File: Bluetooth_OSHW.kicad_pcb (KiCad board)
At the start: 4 copper layers, 45.8 x 19.6 mm, 79 parts, among them J1 Conn_01x15, J2 Conn_01x15, J3 BAT_SOCKET, J4 Conn_ARM_SWD_TagConnect_TC203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, J5 USB_C_Plug_USB2.0, Q1 DMG1012T, U1 STM32WB55RGVx, U3 AT25SL321-U, U4 BQ25185, U5 TPS62746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

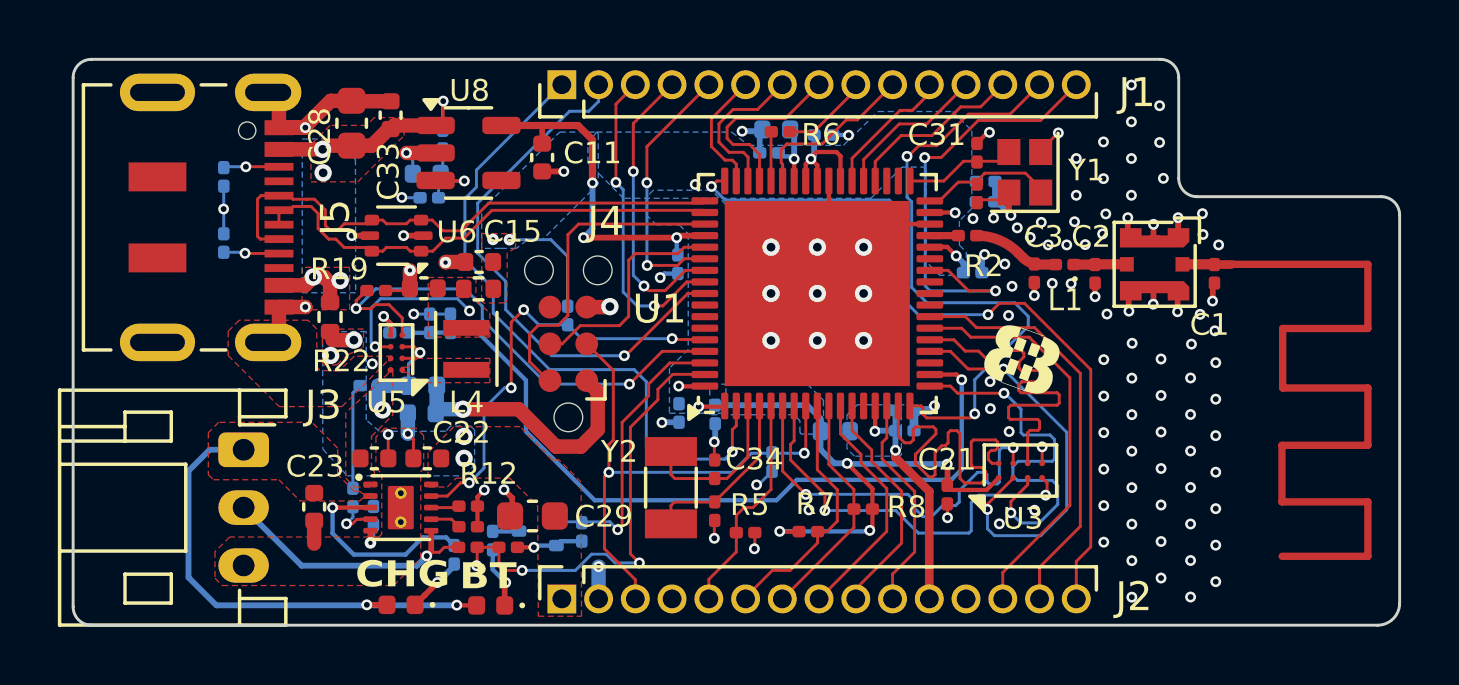
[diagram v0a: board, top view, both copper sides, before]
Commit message: Adding outputs, updated some component values.
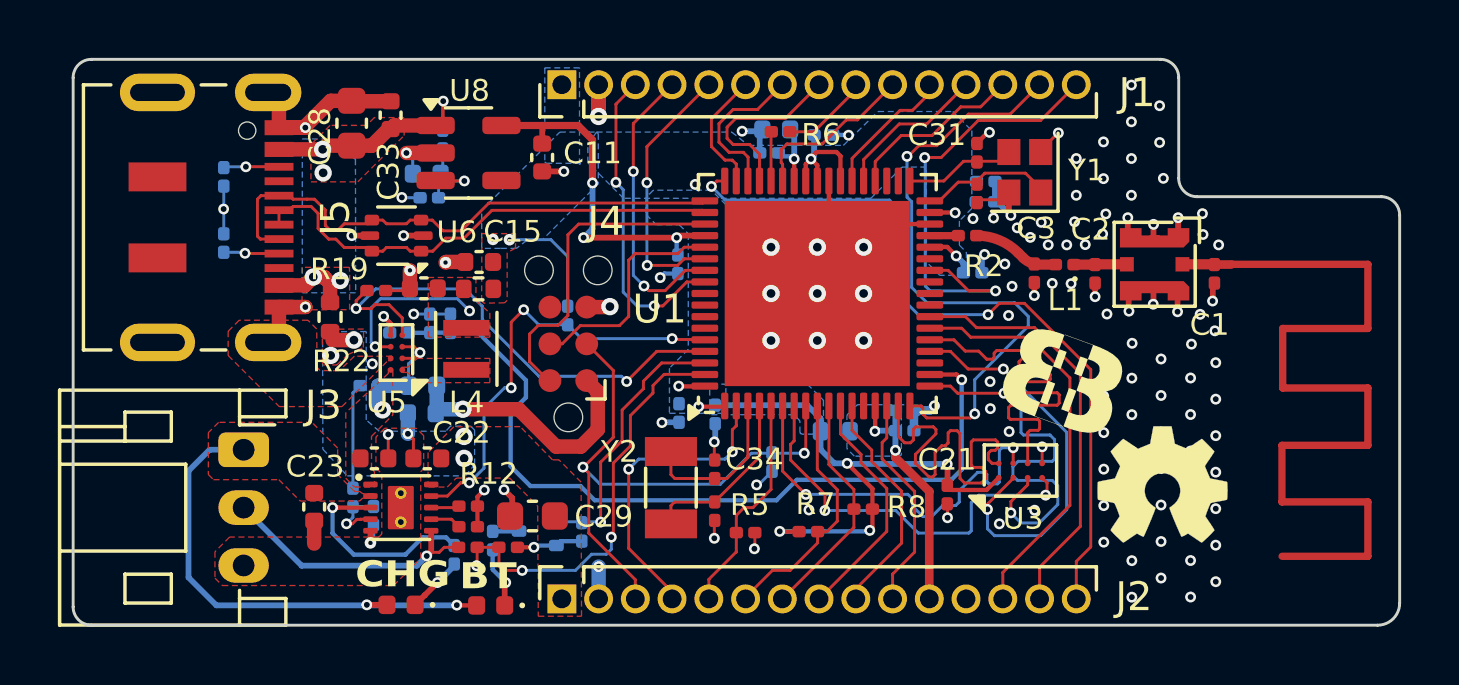
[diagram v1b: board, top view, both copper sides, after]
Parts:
- added REF**: OSHW-Logo_5.7x6mm_SilkScreen, Symbol:OSHW-Logo_5.7x6mm_SilkScreen, F.Cu at (229.0, 143.7)
- C11: value C -> 4.7UF
- D3: value D -> BAT54LP
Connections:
- J1 pad 1: STM_WKUP2_PC13 -> PP1800_ALW
- J1 pad 2: STM_WKUP3_PC12 -> GND
- J2 pad 4: unconnected-(J2-Pin_4-Pad4) -> STM_WKUP2_PC13
- U1 pad 60: STM_WKUP3_PC12 -> unconnected-(U1-PC12-Pad60)
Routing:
- net STM_WKUP3_PC12: track 18.7 -> 0.00 mm, vias 1 -> 0
- net STM_WKUP2_PC13: track 23.1 -> 10.6 mm, vias 1 -> 2
- net GND: track 62.7 -> 64.9 mm, vias 128 -> 129
- net RESETB: track 18.4 -> 20.4 mm
- net VIN_SNS_ADC1_IN9: track 27.3 -> 28.7 mm
- net BAT_CHRG_FACTORY: track 15.7 -> 14.5 mm
- net /BLE_MCU/BT_CONN_LED: track 10.0 -> 9.48 mm
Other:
- board text removed: "${REFERENCE}"

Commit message: updating design files
updating schematics, gerbers, design files, etc.
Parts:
- R16: value 1K -> 2.2K
- moved R4 0.98 mm to (209.0, 137.7), turned to 0 degrees
- moved R24 0.65 mm to (205.9, 145.3)
- moved R3 0.24 mm to (204.6, 145.4)
- moved C29 0.23 mm to (207.5, 143.8)
- moved C9 0.15 mm to (212.2, 135.0)
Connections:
- net QSPI_MEM_CLK renamed /BLE_MCU/QSPI_MEM_CLK
- net QSPI_MEM_CS_L renamed /BLE_MCU/QSPI_MEM_CS_L
- net QSPI_MEM_D0 renamed /BLE_MCU/QSPI_MEM_D0
- net QSPI_MEM_D1 renamed /BLE_MCU/QSPI_MEM_D1
- net QSPI_MEM_D2 renamed /BLE_MCU/QSPI_MEM_D2
- net QSPI_MEM_D3 renamed /BLE_MCU/QSPI_MEM_D3
- J4 pad 6: unconnected-(J4-SWO-Pad6) -> SWD_O
- U1 pad 25: GPIO_PC4 -> unconnected-(U1-PC4-Pad25)
- U1 pad 60: unconnected-(U1-PC12-Pad60) -> SWD_O
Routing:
- net SWD_O: track 0.00 -> 7.79 mm, vias 0 -> 2
- net GND: track 64.9 -> 66.6 mm, vias 129 -> 133
- net PP1800_ALW: track 34.2 -> 35.5 mm
- net Net-(D4-K): track 2.12 -> 1.44 mm
- net BAT_CHRG_FACTORY: track 14.5 -> 13.9 mm, vias 3 -> 2
- net FLT_CHG_L: track 15.1 -> 15.5 mm, vias 4 -> 2
